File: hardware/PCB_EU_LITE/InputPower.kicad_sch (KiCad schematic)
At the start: 17 parts, among them J101 24 V IN, Q102 IRL2505, U102 INA238

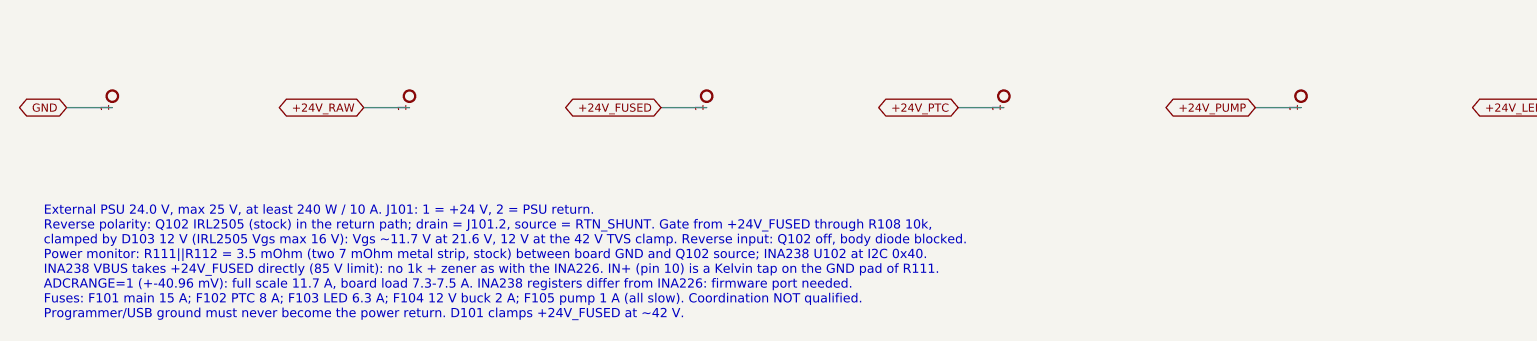
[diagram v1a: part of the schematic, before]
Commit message: Finish EU-LITE LED routing and parallel outputs
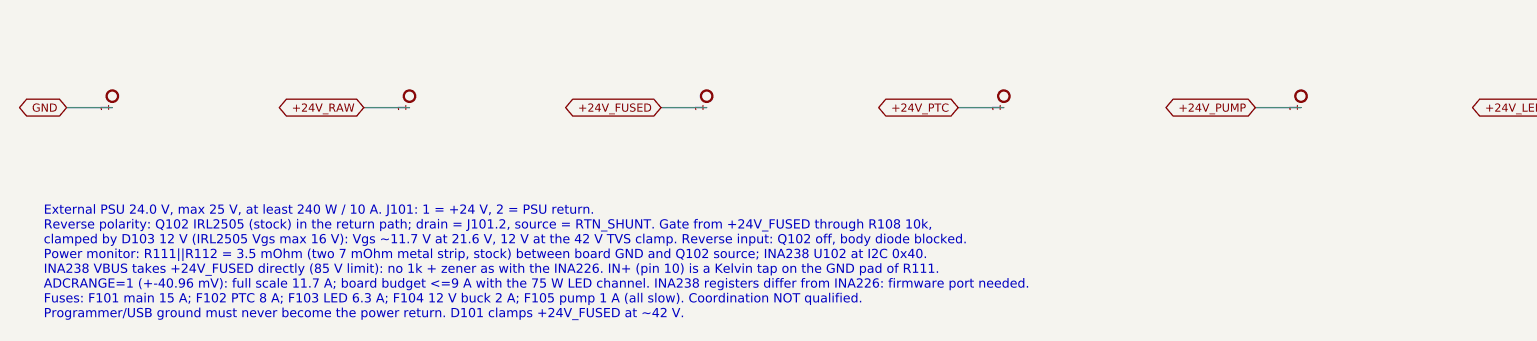
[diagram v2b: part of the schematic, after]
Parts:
- J101: Design_note KF301-5.0-2P: pin 1 +24 V, pin 2 return. Terminal rating (1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 -> KF301-5.0-2P: pin 1 +24 V, pin 2 return. Confirm terminal r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
- Q102: Design_note Stock IRL2505, TO-220 G-D-S, vertical without heatsink (~0.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 -> Stock IRL2505, TO-220 G-D-S, vertical without heatsink. Che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
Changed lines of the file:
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@@
 (kicad_sch (version 20260306) (generator "eeschema") (generator_version "10.0") (paper "A3") (title_block (title "01 | 24 V input, reverse polarity, fuses and power monitor") (date "2026-10-24") (rev "EU-LITE-0.1") (company "GrowBox | EU-LITE from stock") (comment 1 "SCHEMATIC DRAFT | no PCB / manufacturing release"))
 (text "01 | 24 V input, reverse polarity, fuses and power monitor" (at 12.7 12.7 0) (effects (font (size 2 2)) (justify left top)))
-(text "External PSU 24.0 V, max 25 V, at least 240 W / 10 A. J101: 1 = +24 V, 2 = PSU return.\nReverse polarity: Q102 IRL2505 (stock) in the return path; drain = J101.2, source = RTN_SHUNT. Gate from +24V_FUSED through R108 10k,\nclamped by D103 12 V (IRL2505 Vgs max 16 V): Vgs ~11.7 V at 21.6 V, 12 V at the 42 V TVS clamp. Reverse input: Q102 off, body diode blocked.\nPower monitor: R111||R112 = 3.5 mOhm (two 7 mOhm metal strip, stock) between board GND and Q102 source; INA238 U102 at I2C 0x40.\nINA238 VBUS takes +24V_FUSED directly (85 V limit): no 1k + zener as with the INA226. IN+ (pin 10) is a Kelvin tap on the GND pad of R111.\nADCRANGE=1 (+-40.96 mV): full scale 11.7 A, board load 7.3-7.5 A. INA238 registers differ from INA226: firmware port needed.\nFuses: F101 main 15 A; F102 PTC 8 A; F103 LED 6.3 A; F104 12 V buck 2 A; F105 pump 1 A (all slow). Coordination NOT qualified.\nProgrammer/USB ground must never become the power return. D101 clamps +24V_FUSED at ~42 V." (at 12.7 251 0) (effects (font (size 1.02 1.02)) (justify left top)))
+(text "External PSU 24.0 V, max 25 V, at least 240 W / 10 A. J101: 1 = +24 V, 2 = PSU return.\nReverse polarity: Q102 IRL2505 (stock) in the return path; drain = J101.2, source = RTN_SHUNT. Gate from +24V_FUSED through R108 10k,\nclamped by D103 12 V (IRL2505 Vgs max 16 V): Vgs ~11.7 V at 21.6 V, 12 V at the 42 V TVS clamp. Reverse input: Q102 off, body diode blocked.\nPower monitor: R111||R112 = 3.5 mOhm (two 7 mOhm metal strip, stock) between board GND and Q102 source; INA238 U102 at I2C 0x40.\nINA238 VBUS takes +24V_FUSED directly (85 V limit): no 1k + zener as with the INA226. IN+ (pin 10) is a Kelvin tap on the GND pad of R111.\nADCRANGE=1 (+-40.96 mV): full scale 11.7 A; board budget <=9 A with the 75 W LED channel. INA238 registers differ from INA226: firmware port needed.\nFuses: F101 main 15 A; F102 PTC 8 A; F103 LED 6.3 A; F104 12 V buck 2 A; F105 pump 1 A (all slow). Coordination NOT qualified.\nProgrammer/USB ground must never become the power return. D101 clamps +24V_FUSED at ~42 V." (at 12.7 251 0) (effects (font (size 1.02 1.02)) (justify left top)))
 (symbol (lib_id "EU_LITE:J2") (at 45.72 129.54 0) (unit 1) (in_bom yes) (on_board yes) (dnp no)
 (property "Reference" "J101" (at 45.72 122.63 0) (effects (font (size 1.15 1.15)) ))
@@
 (property "MPN" "KF301-5.0-2P" (at 45.72 129.54 0) (effects (font (size 1 1)) (hide yes)))
 (property "Source" "stock:93" (at 45.72 129.54 0) (effects (font (size 1 1)) (hide yes)))
-(property "Design_note" "KF301-5.0-2P: pin 1 +24 V, pin 2 return. Terminal rating (10-16 A) to confirm: board load up to ~7.5 A (9.3 A at 21.6 V is the EU-0.1 budget with 2 LED channels)" (at 45.72 129.54 0) (effects (font (size 1 1)) (hide yes)))
+(property "Design_note" "KF301-5.0-2P: pin 1 +24 V, pin 2 return. Confirm terminal rating: design current envelope 9 A with one 75 W LED channel plus the other loads" (at 45.72 129.54 0) (effects (font (size 1 1)) (hide yes)))
 (property "FootprintStatus" "PACKAGE ONLY - verify before PCB" (at 45.72 129.54 0) (effects (font (size 1 1)) (hide yes)))
 (pin "1")
@@
 (property "MPN" "IRL2505" (at 265.43 199.39 0) (effects (font (size 1 1)) (hide yes)))
 (property "Source" "stock:78" (at 265.43 199.39 0) (effects (font (size 1 1)) (hide yes)))
-(property "Design_note" "Stock IRL2505, TO-220 G-D-S, vertical without heatsink (~0.65 W at 7.5 A). Drain tab = PSU_RTN. Vgs max 16 V: gate is clamped by D103" (at 265.43 199.39 0) (effects (font (size 1 1)) (hide yes)))
+(property "Design_note" "Stock IRL2505, TO-220 G-D-S, vertical without heatsink. Check dissipation at the 9 A board-current envelope. Drain tab = PSU_RTN. Vgs max 16 V: gate is clamped by D103" (at 265.43 199.39 0) (effects (font (size 1 1)) (hide yes)))
 (property "FootprintStatus" "PACKAGE ONLY - verify before PCB" (at 265.43 199.39 0) (effects (font (size 1 1)) (hide yes)))
 (pin "1")

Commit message: Correct F103 USI fast fuse annotation without changing connectivity
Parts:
- F103: value 6.3 A slow -> 6.3 A fast
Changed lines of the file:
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@@
 (kicad_sch (version 20260306) (generator "eeschema") (generator_version "10.0") (paper "A3") (title_block (title "01 | 24 V input, reverse polarity, fuses and power monitor") (date "2026-10-24") (rev "EU-LITE-0.1") (company "GrowBox | EU-LITE from stock") (comment 1 "SCHEMATIC DRAFT | no PCB / manufacturing release"))
 (text "01 | 24 V input, reverse polarity, fuses and power monitor" (at 12.7 12.7 0) (effects (font (size 2 2)) (justify left top)))
-(text "External PSU 24.0 V, max 25 V, at least 240 W / 10 A. J101: 1 = +24 V, 2 = PSU return.\nReverse polarity: Q102 IRL2505 (stock) in the return path; drain = J101.2, source = RTN_SHUNT. Gate from +24V_FUSED through R108 10k,\nclamped by D103 12 V (IRL2505 Vgs max 16 V): Vgs ~11.7 V at 21.6 V, 12 V at the 42 V TVS clamp. Reverse input: Q102 off, body diode blocked.\nPower monitor: R111||R112 = 3.5 mOhm (two 7 mOhm metal strip, stock) between board GND and Q102 source; INA238 U102 at I2C 0x40.\nINA238 VBUS takes +24V_FUSED directly (85 V limit): no 1k + zener as with the INA226. IN+ (pin 10) is a Kelvin tap on the GND pad of R111.\nADCRANGE=1 (+-40.96 mV): full scale 11.7 A; board budget <=9 A with the 75 W LED channel. INA238 registers differ from INA226: firmware port needed.\nFuses: F101 main 15 A; F102 PTC 8 A; F103 LED 6.3 A; F104 12 V buck 2 A; F105 pump 1 A (all slow). Coordination NOT qualified.\nProgrammer/USB ground must never become the power return. D101 clamps +24V_FUSED at ~42 V." (at 12.7 251 0) (effects (font (size 1.02 1.02)) (justify left top)))
+(text "External PSU 24.0 V, max 25 V, at least 240 W / 10 A. J101: 1 = +24 V, 2 = PSU return.\nReverse polarity: Q102 IRL2505 (stock) in the return path; drain = J101.2, source = RTN_SHUNT. Gate from +24V_FUSED through R108 10k,\nclamped by D103 12 V (IRL2505 Vgs max 16 V): Vgs ~11.7 V at 21.6 V, 12 V at the 42 V TVS clamp. Reverse input: Q102 off, body diode blocked.\nPower monitor: R111||R112 = 3.5 mOhm (two 7 mOhm metal strip, stock) between board GND and Q102 source; INA238 U102 at I2C 0x40.\nINA238 VBUS takes +24V_FUSED directly (85 V limit): no 1k + zener as with the INA226. IN+ (pin 10) is a Kelvin tap on the GND pad of R111.\nADCRANGE=1 (+-40.96 mV): full scale 11.7 A; board budget <=9 A with the 75 W LED channel. INA238 registers differ from INA226: firmware port needed.\nFuses: F101 main 15 A; F102 PTC 8 A; F103 LED 6.3 A USI fast; F104 12 V buck 2 A; F105 pump 1 A (all except F103 slow). Coordination NOT qualified.\nProgrammer/USB ground must never become the power return. D101 clamps +24V_FUSED at ~42 V." (at 12.7 251 0) (effects (font (size 1.02 1.02)) (justify left top)))
 (symbol (lib_id "EU_LITE:J2") (at 45.72 129.54 0) (unit 1) (in_bom yes) (on_board yes) (dnp no)
 (property "Reference" "J101" (at 45.72 122.63 0) (effects (font (size 1.15 1.15)) ))
@@
 (symbol (lib_id "EU_LITE:F") (at 241.3 129.54 0) (unit 1) (in_bom yes) (on_board yes) (dnp no)
 (property "Reference" "F103" (at 241.3 123.9 0) (effects (font (size 1.15 1.15)) ))
-(property "Value" "6.3 A slow" (at 241.3 135.18 0) (effects (font (size 0.98 0.98)) ))
+(property "Value" "6.3 A fast" (at 241.3 135.18 0) (effects (font (size 0.98 0.98)) ))
 (property "Footprint" "EU_Mechanical:Fuse_Schurter_UST_USI1206_Reflow" (at 241.3 129.54 0) (effects (font (size 1 1)) (hide yes)))
 (property "Datasheet" "" (at 241.3 129.54 0) (effects (font (size 1 1)) (hide yes)))
